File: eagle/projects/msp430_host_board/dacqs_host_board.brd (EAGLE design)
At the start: 127 x 100 mm, 272 parts, among them J1 MOL-SL-4-RA, J10 MOL-SL-3-V, J11 MOL-SL-2-V, J12 CONN HEADER 20POS .100" DBL, J13 MOL-SL-2-RA, J14 USB_MICROB_RECPT, J16 MOL-SL-2-RA, J17 CLM-112-02-L-D-IMU-MOUNT_IMU, J18 MOLSL-7-RA, J19 CONN HEADER 20POS .100" DBL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

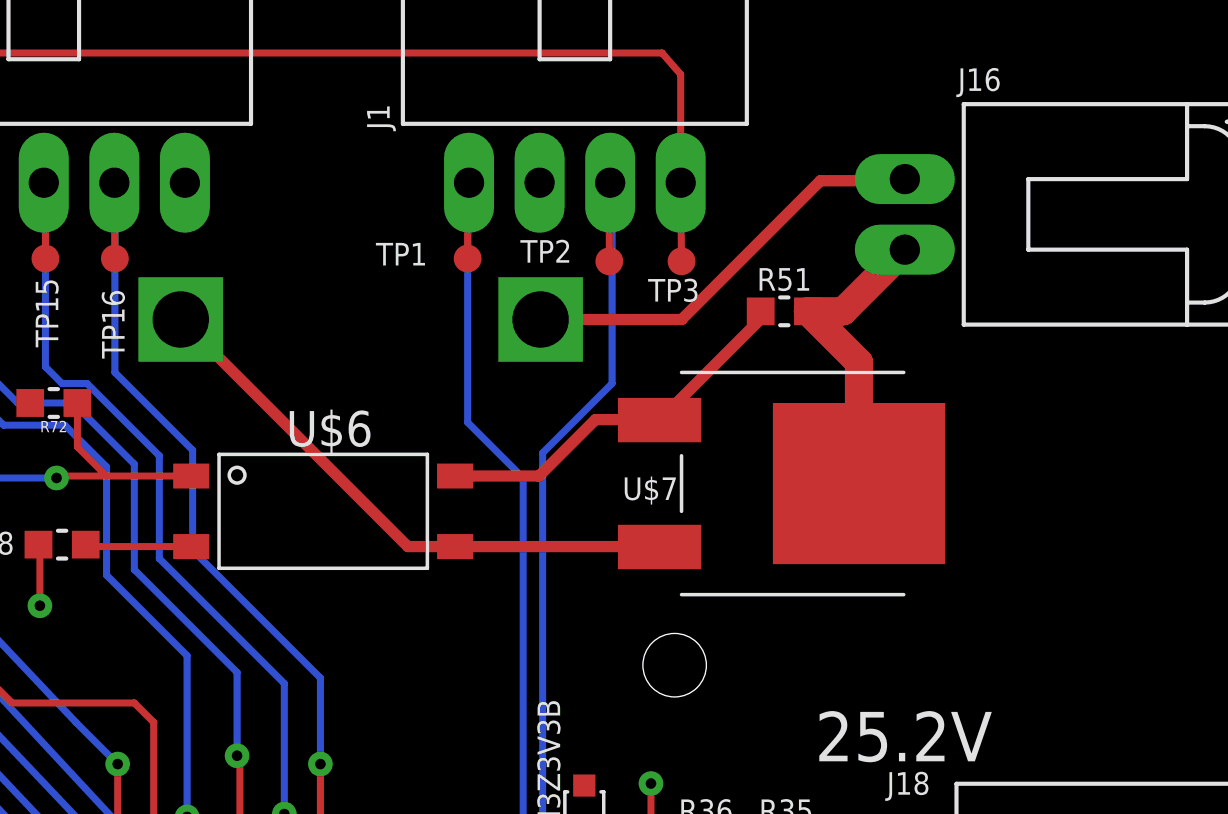
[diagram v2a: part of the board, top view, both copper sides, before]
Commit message: Fixed the power mosfet mixup
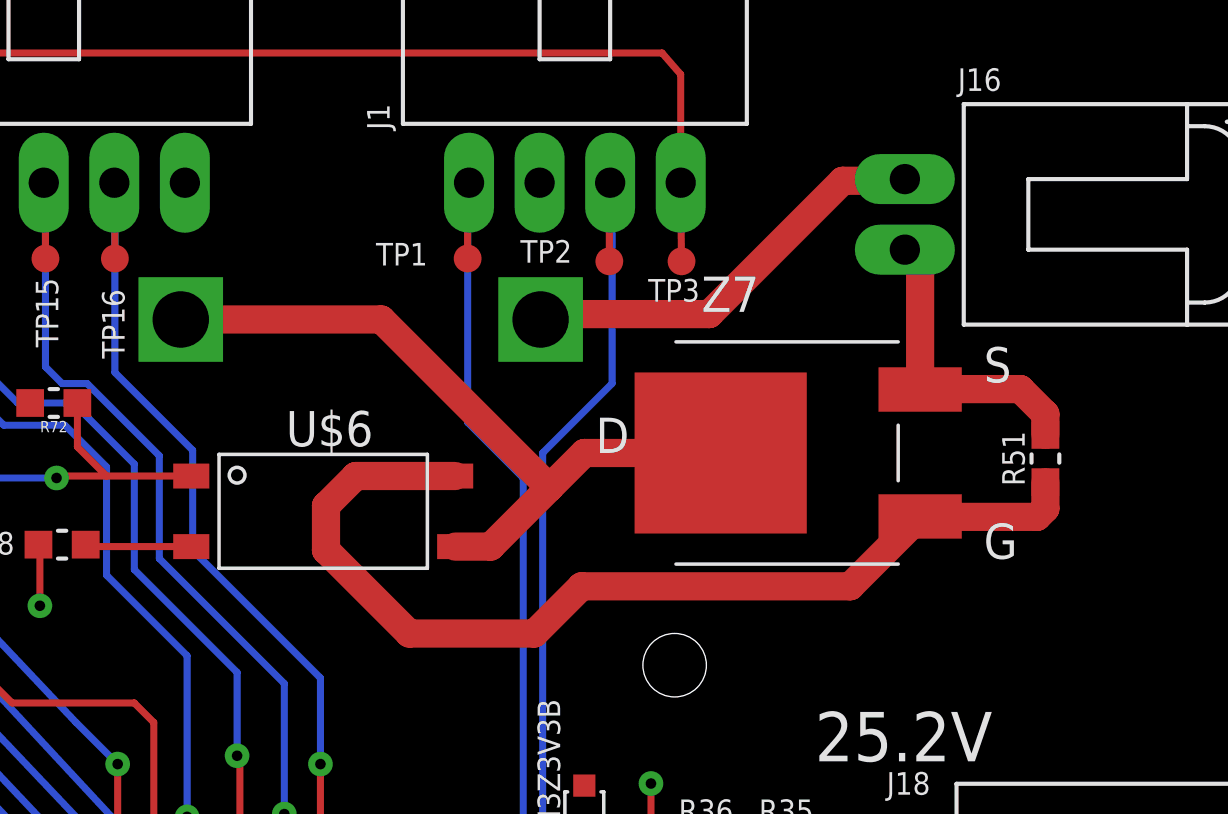
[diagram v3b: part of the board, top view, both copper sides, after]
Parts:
- removed U$7: NTD2955T4G, daqcs_host:NTD2955T4G
- added Z7: (no value), daqcs_host:NTD2955T4G
- moved R51 10.8 mm to (118.4, 77.4), turned to 90 degrees
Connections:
- net 9V_GND: now also Z7.P$3; no longer U$7.P$2
- net CUTDOWN_DRAIN: now also Z7.P$2; no longer U$7.P$3
- net CUTDOWN_GATE: now also Z7.P$1; no longer U$7.P$1
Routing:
- net CUTDOWN_GATE: track 13.6 -> 36.7 mm
- net 9V_GND: track 20.6 -> 26.7 mm
- net CUTDOWN_DRAIN: track 11.5 -> 10.9 mm
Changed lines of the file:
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@@
 <layer number="14" name="Route14" color="1" fill="6" visible="no" active="no"/>
 <layer number="15" name="Route15" color="4" fill="6" visible="yes" active="yes"/>
-<layer number="16" name="Bottom" color="1" fill="1" visible="yes" active="yes"/>
+<layer number="16" name="Bottom" color="1" fill="1" visible="no" active="yes"/>
 <layer number="17" name="Pads" color="2" fill="1" visible="yes" active="yes"/>
 <layer number="18" name="Vias" color="2" fill="1" visible="yes" active="yes"/>
@@
 <attribute name="VALUE" x="87.83" y="71.59" size="1.27" layer="27"/>
 </element>
-<element name="U$7" library="daqcs_host" package="NTD2955T4G" value="NTD2955T4G" x="107.3" y="76.5" smashed="yes" rot="R180">
-<attribute name="MANUFACTURER" value="ON Semiconductor" x="107.3" y="76.5" size="1.778" layer="27" rot="R180" display="off"/>
-<attribute name="VENDOR" value="Digi-key" x="107.3" y="76.5" size="1.778" layer="27" rot="R180" display="off"/>
-<attribute name="VENDOR_PN" value="NTD2955T4GOSCT-ND " x="107.3" y="76.5" size="1.778" layer="27" rot="R180" display="off"/>
-<attribute name="MANUFACTURER_PN" value="NTD2955T4G" x="107.3" y="76.5" size="1.778" layer="27" rot="R180" display="off"/>
-<attribute name="NAME" x="105.18" y="76.72" size="0.8128" layer="25" ratio="15" rot="R180"/>
-<attribute name="VALUE" x="125.28" y="81.25" size="1.27" layer="27" rot="R180"/>
-</element>
-<element name="R51" library="daqcs_host" package="R0603" value="47k" x="109" y="82.7" smashed="yes">
-<attribute name="MANUFACTURER" value="Panasonic" x="109" y="82.7" size="1.778" layer="27" display="off"/>
-<attribute name="VENDOR" value="Digi-key" x="109" y="82.7" size="1.778" layer="27" display="off"/>
-<attribute name="VENDOR_PN" value="P47.0KHCT-ND" x="109" y="82.7" size="1.778" layer="27" display="off"/>
-<attribute name="TOLERANCE" value="1%" x="109" y="82.7" size="1.778" layer="27" display="off"/>
-<attribute name="MANUFACTURER_PN" value="ERJ-3EKF4702V" x="109" y="82.7" size="1.778" layer="27" display="off"/>
-<attribute name="POWER" value="1/10W" x="109" y="82.7" size="1.778" layer="27" display="off"/>
-<attribute name="NAME" x="109" y="83.85" size="0.8128" layer="25" ratio="15" align="center"/>
-<attribute name="VALUE" x="109" y="81.95" size="0.254" layer="27" ratio="6" align="center"/>
+<element name="R51" library="daqcs_host" package="R0603" value="47k" x="118.4" y="77.4" smashed="yes" rot="R90">
+<attribute name="MANUFACTURER" value="Panasonic" x="118.4" y="77.4" size="1.778" layer="27" rot="R90" display="off"/>
+<attribute name="VENDOR" value="Digi-key" x="118.4" y="77.4" size="1.778" layer="27" rot="R90" display="off"/>
+<attribute name="VENDOR_PN" value="P47.0KHCT-ND" x="118.4" y="77.4" size="1.778" layer="27" rot="R90" display="off"/>
+<attribute name="TOLERANCE" value="1%" x="118.4" y="77.4" size="1.778" layer="27" rot="R90" display="off"/>
+<attribute name="MANUFACTURER_PN" value="ERJ-3EKF4702V" x="118.4" y="77.4" size="1.778" layer="27" rot="R90" display="off"/>
+<attribute name="POWER" value="1/10W" x="118.4" y="77.4" size="1.778" layer="27" rot="R90" display="off"/>
+<attribute name="NAME" x="117.25" y="77.4" size="0.8128" layer="25" ratio="15" rot="R90" align="center"/>
+<attribute name="VALUE" x="119.15" y="77.4" size="0.254" layer="27" ratio="6" rot="R90" align="center"/>
 </element>
 <element name="R28" library="daqcs_host" package="R0603" value="2k" x="83" y="74.3" smashed="yes">
@@
 <attribute name="TOLERANCE" value="1%" x="82.7" y="79.4" size="1.778" layer="27" rot="R180" display="off"/>
 </element>
+<element name="Z7" library="daqcs_host" package="NTD2955T4G" value="" x="111.1" y="77.6">
+<attribute name="VENDOR" value="Digi-key" x="111.1" y="77.6" size="1.778" layer="27" display="off"/>
+<attribute name="VENDOR_PN" value="NTD2955T4GOSCT-ND " x="111.1" y="77.6" size="1.778" layer="27" display="off"/>
+<attribute name="MANUFACTURER" value="ON Semiconductor" x="111.1" y="77.6" size="1.778" layer="27" display="off"/>
+<attribute name="MANUFACTURER_PN" value="NTD2955T4G" x="111.1" y="77.6" size="1.778" layer="27" display="off"/>
+</element>
 </elements>
 <signals>
@@
 <contactref element="BAT1" pad="V+"/>
 <contactref element="J16" pad="1"/>
-<wire x1="100.226" y1="82.406" x2="105.306" y2="82.406" width="0.4064" layer="1"/>
-<wire x1="105.306" y1="82.406" x2="110.3" y2="87.4" width="0.4064" layer="1"/>
-<wire x1="110.3" y1="87.4" x2="113.28" y2="87.4" width="0.4064" layer="1"/>
 <wire x1="113.28" y1="87.4" x2="113.34" y2="87.46" width="0.4064" layer="1"/>
+<wire x1="113.28" y1="87.4" x2="111.1" y2="87.4" width="1.016" layer="1"/>
+<wire x1="111.1" y1="87.4" x2="106.3" y2="82.6" width="1.016" layer="1"/>
+<wire x1="106.3" y1="82.6" x2="100.42" y2="82.6" width="1.016" layer="1"/>
+<wire x1="100.42" y1="82.6" x2="100.226" y2="82.406" width="1.016" layer="1"/>
 </signal>
 <signal name="CUTDOWN_DRAIN">
 <contactref element="J16" pad="2"/>
 <contactref element="R51" pad="2"/>
-<contactref element="U$7" pad="P$3"/>
-<wire x1="109.9" y1="82.579290625" x2="109.85" y2="82.7" width="0.8128" layer="1" curve="45"/>
-<wire x1="111.69" y1="76.5" x2="111.69" y2="80.86" width="1.016" layer="1"/>
-<wire x1="111.69" y1="80.86" x2="109.85" y2="82.7" width="1.016" layer="1"/>
-<wire x1="109.85" y1="82.7" x2="111.12" y2="82.7" width="1.016" layer="1"/>
-<wire x1="111.12" y1="82.7" x2="113.34" y2="84.92" width="1.016" layer="1"/>
+<contactref element="Z7" pad="P$2"/>
+<wire x1="118.4" y1="78.25" x2="118.4" y2="79" width="1.016" layer="1"/>
+<wire x1="118.4" y1="79" x2="117.5" y2="79.9" width="1.016" layer="1"/>
+<wire x1="117.5" y1="79.9" x2="113.905" y2="79.9" width="1.016" layer="1"/>
+<wire x1="113.905" y1="79.9" x2="113.89" y2="79.885" width="1.016" layer="1"/>
+<wire x1="113.89" y1="79.885" x2="113.89" y2="84.37" width="1.016" layer="1"/>
+<wire x1="113.89" y1="84.37" x2="113.34" y2="84.92" width="1.016" layer="1"/>
 </signal>
 <signal name="TEMP_I2C_A0">
@@
 <signal name="9V_GND">
 <contactref element="BAT1" pad="V-"/>
-<contactref element="U$7" pad="P$2"/>
 <contactref element="U$6" pad="P$3"/>
-<wire x1="97.15" y1="74.23" x2="95.448" y2="74.23" width="0.4064" layer="1"/>
-<wire x1="95.448" y1="74.23" x2="87.272" y2="82.406" width="0.4064" layer="1"/>
-<wire x1="97.15" y1="74.23" x2="104.495" y2="74.23" width="0.4064" layer="1"/>
-<wire x1="104.495" y1="74.23" x2="104.51" y2="74.215" width="0.4064" layer="1"/>
+<contactref element="Z7" pad="P$3"/>
+<wire x1="97.15" y1="74.23" x2="98.43" y2="74.23" width="1.016" layer="1"/>
+<wire x1="98.43" y1="74.23" x2="100.55" y2="76.35" width="1.016" layer="1"/>
+<wire x1="100.55" y1="76.35" x2="101.8" y2="77.6" width="1.016" layer="1"/>
+<wire x1="101.8" y1="77.6" x2="106.71" y2="77.6" width="1.016" layer="1"/>
+<wire x1="87.272" y1="82.406" x2="94.494" y2="82.406" width="1.016" layer="1"/>
+<wire x1="94.494" y1="82.406" x2="100.55" y2="76.35" width="1.016" layer="1"/>
 </signal>
 <signal name="OPTO_OUT">
@@
 </signal>
 <signal name="CUTDOWN_GATE">
-<contactref element="U$7" pad="P$1"/>
 <contactref element="R51" pad="1"/>
 <contactref element="U$6" pad="P$4"/>
-<wire x1="97.15" y1="76.77" x2="100.17" y2="76.77" width="0.4064" layer="1"/>
-<wire x1="100.17" y1="76.77" x2="102.2" y2="78.8" width="0.4064" layer="1"/>
-<wire x1="102.2" y1="78.8" x2="104.495" y2="78.8" width="0.4064" layer="1"/>
-<wire x1="104.495" y1="78.8" x2="104.51" y2="78.785" width="0.4064" layer="1"/>
-<wire x1="108.15" y1="82.7" x2="108.15" y2="82.425" width="0.4064" layer="1"/>
-<wire x1="108.15" y1="82.425" x2="104.51" y2="78.785" width="0.4064" layer="1"/>
+<contactref element="Z7" pad="P$1"/>
+<wire x1="118.4" y1="76.55" x2="118.4" y2="75.6" width="1.016" layer="1"/>
+<wire x1="118.4" y1="75.6" x2="118.1" y2="75.3" width="1.016" layer="1"/>
+<wire x1="118.1" y1="75.3" x2="113.905" y2="75.3" width="1.016" layer="1"/>
+<wire x1="113.905" y1="75.3" x2="113.89" y2="75.315" width="1.016" layer="1"/>
+<wire x1="97.15" y1="76.77" x2="93.57" y2="76.77" width="1.016" layer="1"/>
+<wire x1="93.57" y1="76.77" x2="92.5" y2="75.7" width="1.016" layer="1"/>
+<wire x1="92.5" y1="75.7" x2="92.5" y2="74.1" width="1.016" layer="1"/>
+<wire x1="92.5" y1="74.1" x2="95.5" y2="71.1" width="1.016" layer="1"/>
+<wire x1="95.5" y1="71.1" x2="100" y2="71.1" width="1.016" layer="1"/>
+<wire x1="100" y1="71.1" x2="101.7" y2="72.8" width="1.016" layer="1"/>
+<wire x1="101.7" y1="72.8" x2="111.375" y2="72.8" width="1.016" layer="1"/>
+<wire x1="111.375" y1="72.8" x2="113.89" y2="75.315" width="1.016" layer="1"/>
 </signal>
 <signal name="SPEED_PWM_OUT_0">
